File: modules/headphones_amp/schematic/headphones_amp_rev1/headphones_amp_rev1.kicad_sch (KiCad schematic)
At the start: 7 parts, among them Q1 BC140, Q2 BC160

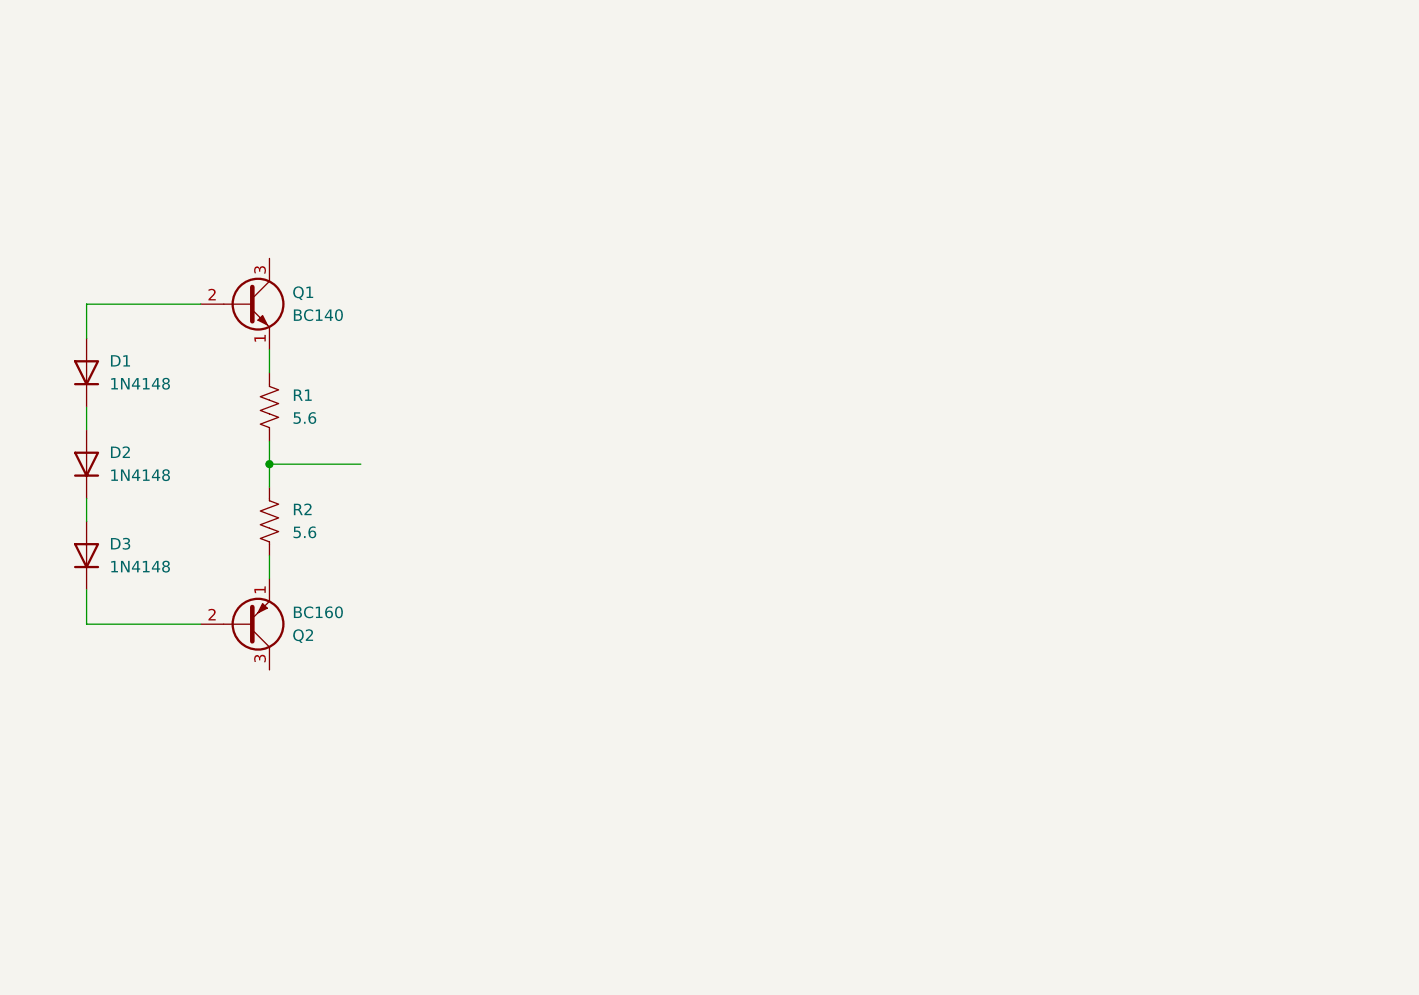
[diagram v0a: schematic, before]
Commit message: updated schematic for the headphones amp and VCF
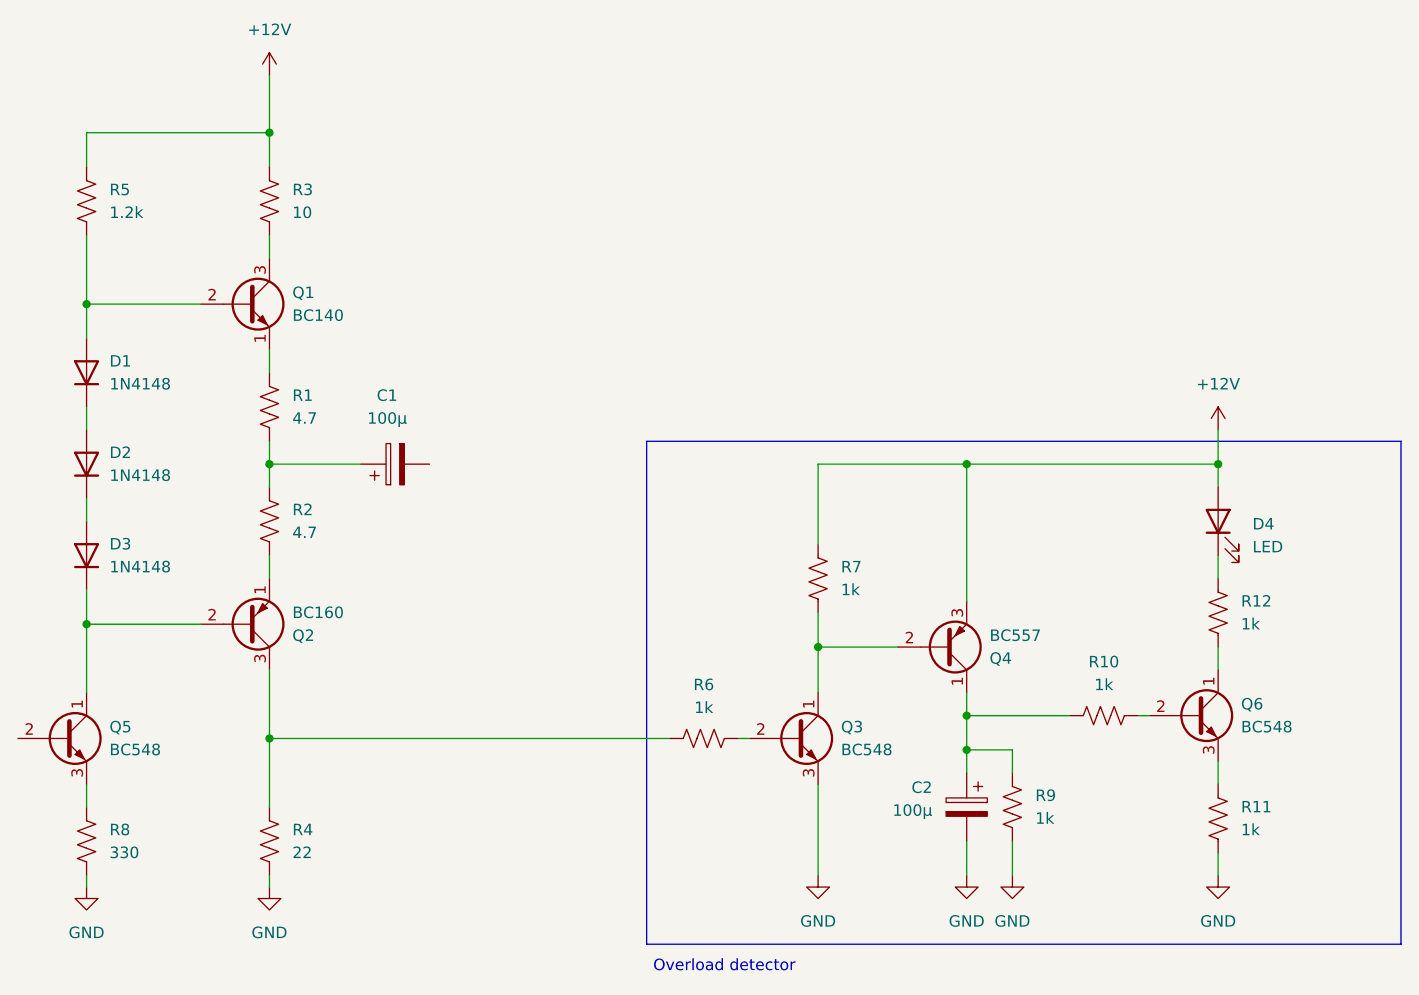
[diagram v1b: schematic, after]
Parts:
- added C1, C2: 100µ, Capacitor_THT:CP_Radial_D10.0mm_P5.00mm, symbol Device:C_Polarized
- added D4: LED, LED_THT:LED_D3.0mm, symbol Device:LED
- added Q3, Q5, Q6: BC548, Package_TO_SOT_THT:TO-92L_Inline_Wide, symbol Transistor_BJT:BC548
- added Q4: BC557, Package_TO_SOT_THT:TO-92L_Inline_Wide, symbol Transistor_BJT:BC557
- added R10, R11, R12, R6, R7, R9: 1k, Resistor_THT:R_Axial_DIN0207_L6.3mm_D2.5mm_P10.16mm_Horizontal, symbol Device:R_US
- added R3: 10, Resistor_THT:R_Axial_DIN0207_L6.3mm_D2.5mm_P10.16mm_Horizontal, symbol Device:R_US
- added R4: 22, Resistor_THT:R_Axial_DIN0207_L6.3mm_D2.5mm_P10.16mm_Horizontal, symbol Device:R_US
- added R5: 1.2k, Resistor_THT:R_Axial_DIN0207_L6.3mm_D2.5mm_P10.16mm_Horizontal, symbol Device:R_US
- added R8: 330, Resistor_THT:R_Axial_DIN0207_L6.3mm_D2.5mm_P10.16mm_Horizontal, symbol Device:R_US
- R1, R2: value 5.6 -> 4.7
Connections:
- net at R1.2, R2.1: now also C1.1
- net at D1.2 (A), Q1.2 (B): now also R5.2
- net at D3.1 (K), Q2.2 (B): now also Q5.1 (C)
- net at Q2.3 (C): now also R4.1, R6.1
- net at Q1.3 (C): now also R3.2
- new net: Q3.1 (C), Q4.2 (B), R7.2
- new net: Q3.2 (B), R6.2
- new net: C2.1, Q4.1 (C), R10.1, R9.1
- new net: D4.1 (K), R12.1
- new net: Q6.1 (C), R12.2
- new net: Q6.2 (B), R10.2
- new net: Q6.3 (E), R11.1
- new net: Q5.3 (E), R8.1
- new net +12V: D4.2 (A), Q4.3 (E), R3.1, R5.1, R7.1
- new net GND: C2.2, Q3.3 (E), R11.2, R4.2, R8.2, R9.2
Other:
- note added: "Overload detector"
- company: (none) -> QuBi
- title: (none) -> Headphone Amplifier
